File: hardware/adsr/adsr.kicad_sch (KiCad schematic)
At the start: 61 parts, among them J1 MonoJack, J2 MonoJack, J4 Conn_02x05_Odd_Even, Q1 BC847, Q2 BC847, Q3 BC847, Q4 BC847, Q5 BC847, Q6 2N7002K, SW1 SW_DPDT_x2, SW2 SW_Push, U1 ICM7556, U2 TL074

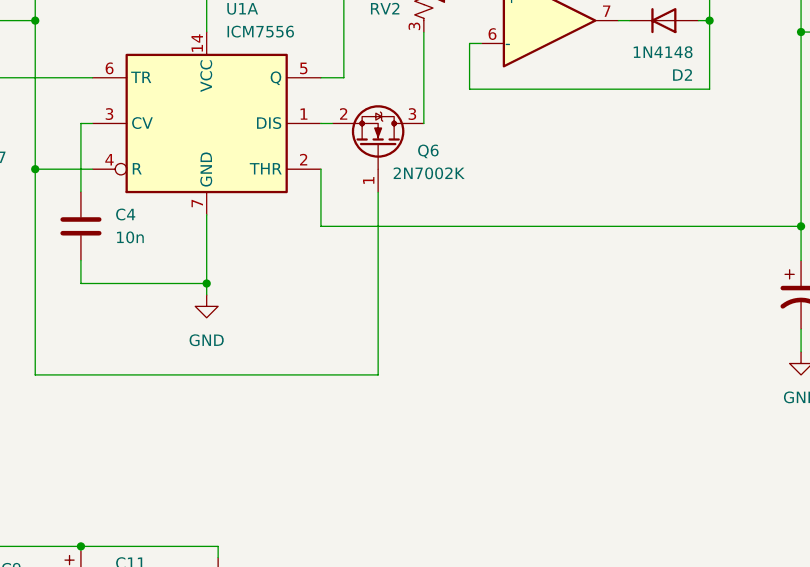
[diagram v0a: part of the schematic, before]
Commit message: Added missing gate R on MOSFET
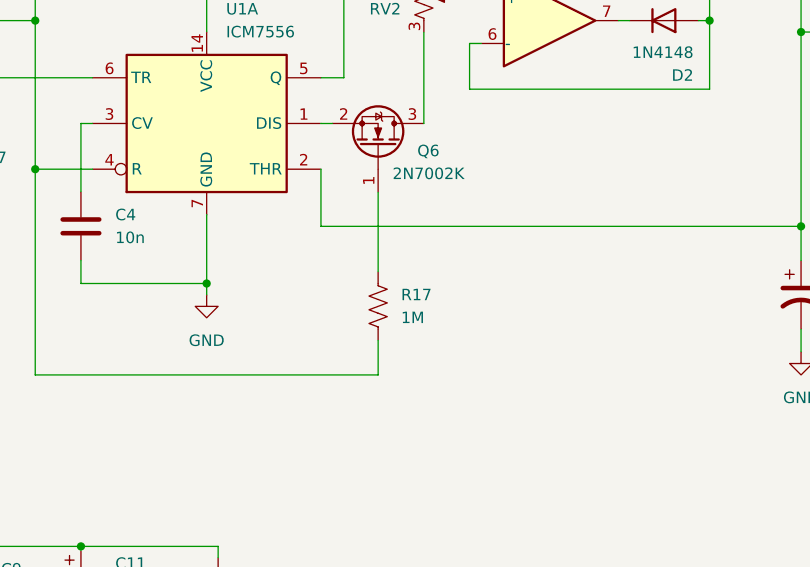
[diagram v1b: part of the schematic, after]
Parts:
- added R17: 1M, Resistor_SMD:R_0805_2012Metric_Pad1.20x1.40mm_HandSolder, symbol Device:R_US
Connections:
- net at C3.2, SW1.2 (B), U1.4 (R)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: now also R17.2; no longer Q6.1 (G)
- new net: Q6.1 (G), R17.1
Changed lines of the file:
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@@
 	(wire
 		(pts
+			(xy 180.34 137.16) (xy 180.34 128.27)
+		)
+		(stroke
+			(width 0)
+			(type default)
+		)
+	)
+	(wire
+		(pts
 			(xy 134.62 185.42) (xy 147.32 185.42)
 		)
@@
 	(wire
 		(pts
-			(xy 180.34 148.59) (xy 180.34 128.27)
+			(xy 180.34 148.59) (xy 180.34 144.78)
 		)
 		(stroke
@@
 					(unit 1)
 				)
+			)
+		)
+	)
+	(symbol
+		(lib_id "Device:R_US")
+		(at 180.34 140.97 0)
+		(unit 1)
+		(exclude_from_sim no)
+		(in_bom yes)
+		(on_board yes)
+		(dnp no)
+		(fields_autoplaced yes)
+		(property "Reference" "R17"
+			(at 182.88 139.6999 0)
+			(effects
+				(font
+					(size 1.27 1.27)
+				)
+				(justify left)
+			)
+		)
+		(property "Value" "1M"
+			(at 182.88 142.2399 0)
+			(effects
+				(font
+					(size 1.27 1.27)
+				)
+				(justify left)
+			)
+		)
+		(property "Footprint" "Resistor_SMD:R_0805_2012Metric_Pad1.20x1.40mm_HandSolder"
+			(at 181.356 141.224 90)
+			(effects
+				(font
+					(size 1.27 1.27)
+				)
+				(hide yes)
+			)
+		)
+		(property "Datasheet" "~"
+			(at 180.34 140.97 0)
+			(effects
+				(font
+					(size 1.27 1.27)
+				)
+				(hide yes)
+			)
+		)
+		(property "Description" "Resistor, US symbol"
+			(at 180.34 140.97 0)
+			(effects
+				(font
+					(size 1.27 1.27)
+				)
+				(hide yes)
+			)
+		)
+		(pin "1"
+		)
+		(pin "2"
+		)
+		(instances
+			(project "adsr"
+				(path "/bc327a33-f4cb-4cb8-a280-c2a5130340fc"
+					(reference "R17")
+					(unit 1)
+				)

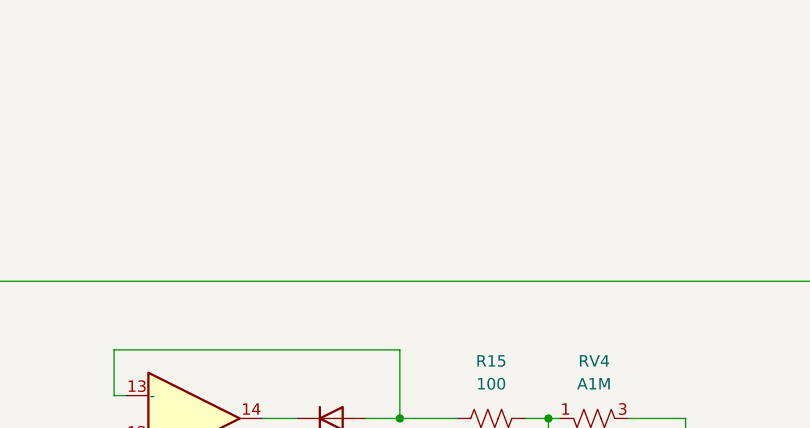
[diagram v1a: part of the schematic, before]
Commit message: added mechanical hole and final silk cleanup
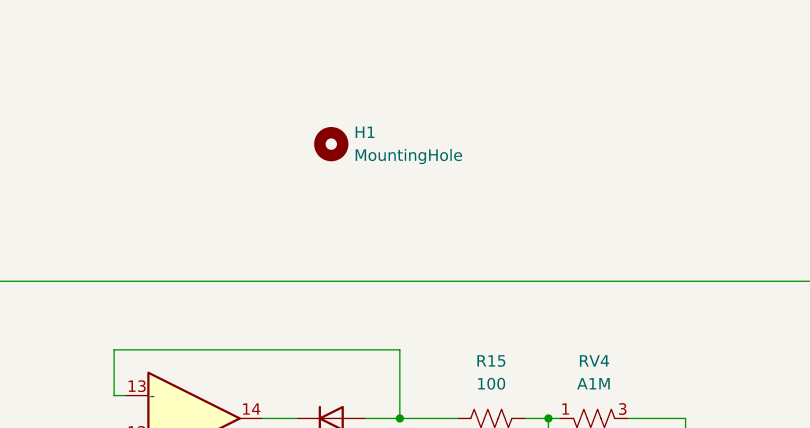
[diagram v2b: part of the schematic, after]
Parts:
- added H1: MountingHole, MountingHole:MountingHole_3.2mm_M3_DIN965, symbol Mechanical:MountingHole
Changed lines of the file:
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@@
+	)
+	(symbol
+		(lib_id "Mechanical:MountingHole")
+		(at 187.96 27.94 0)
+		(unit 1)
+		(exclude_from_sim no)
+		(in_bom no)
+		(on_board yes)
+		(dnp no)
+		(fields_autoplaced yes)
+		(property "Reference" "H1"
+			(at 190.5 26.6699 0)
+			(effects
+				(font
+					(size 1.27 1.27)
+				)
+				(justify left)
+			)
+		)
+		(property "Value" "MountingHole"
+			(at 190.5 29.2099 0)
+			(effects
+				(font
+					(size 1.27 1.27)
+				)
+				(justify left)
+			)
+		)
+		(property "Footprint" "MountingHole:MountingHole_3.2mm_M3_DIN965"
+			(at 187.96 27.94 0)
+			(effects
+				(font
+					(size 1.27 1.27)
+				)
+				(hide yes)
+			)
+		)
+		(property "Datasheet" "~"
+			(at 187.96 27.94 0)
+			(effects
+				(font
+					(size 1.27 1.27)
+				)
+				(hide yes)
+			)
+		)
+		(property "Description" "Mounting Hole without connection"
+			(at 187.96 27.94 0)
+			(effects
+				(font
+					(size 1.27 1.27)
+				)
+				(hide yes)
+			)
+		)
+		(instances
+			(project ""
+				(path "/bc327a33-f4cb-4cb8-a280-c2a5130340fc"
+					(reference "H1")
+					(unit 1)
+				)
+			)
+		)
 	)
 	(symbol

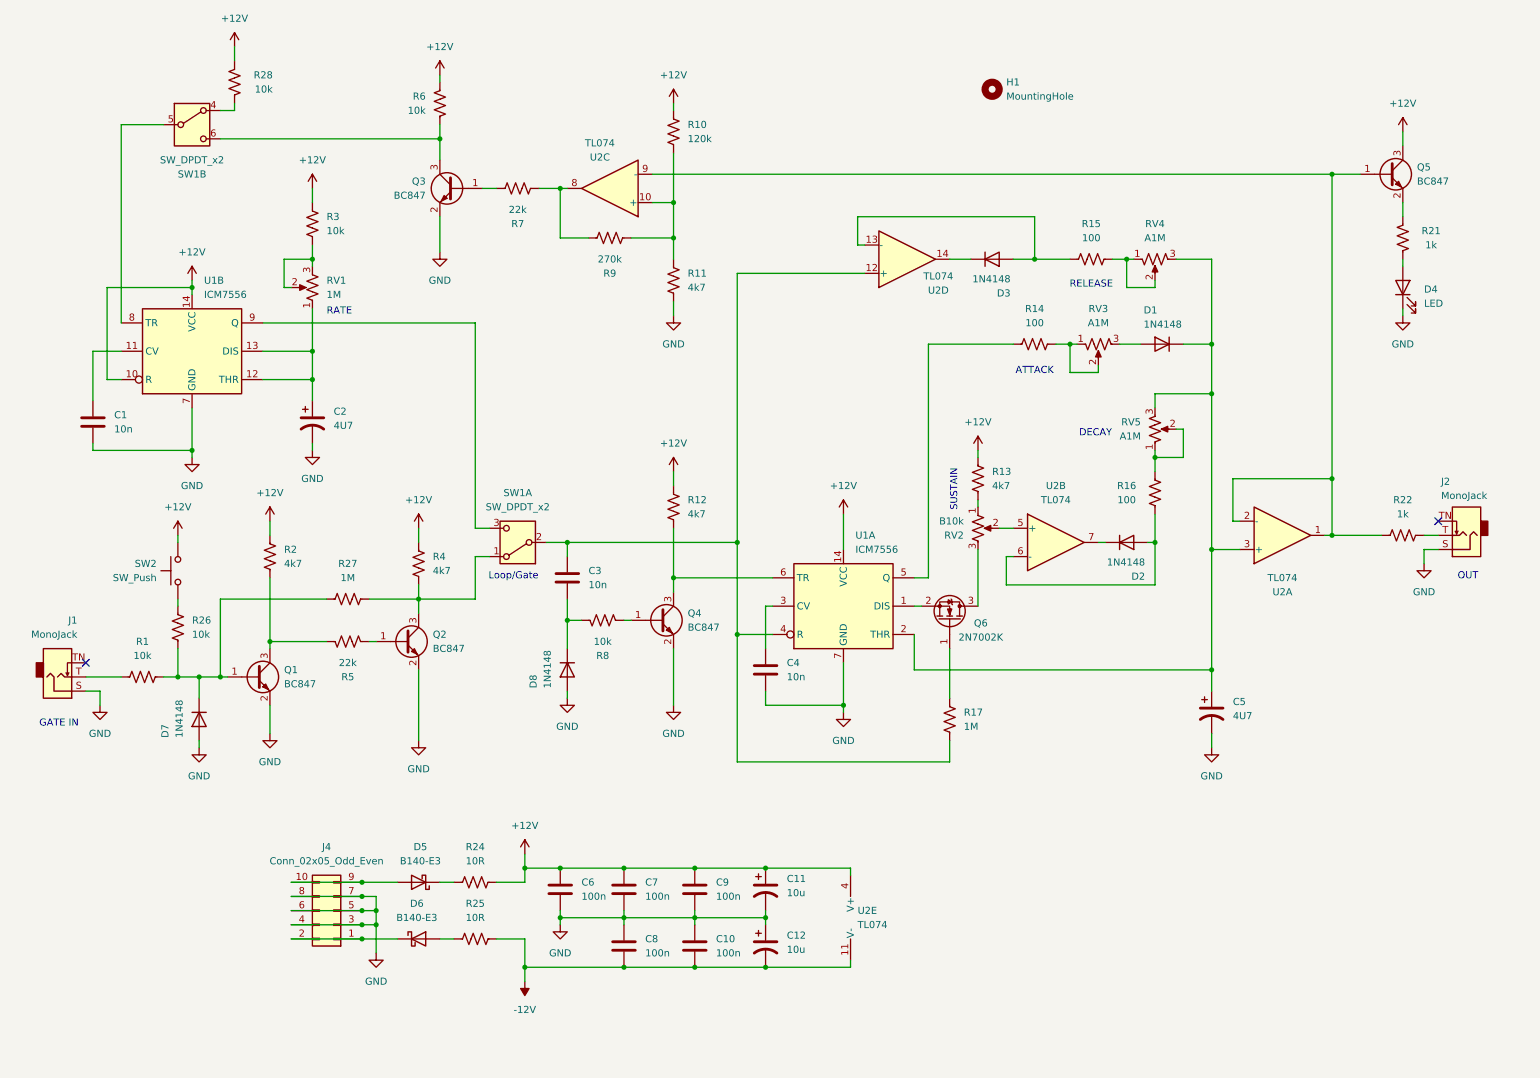
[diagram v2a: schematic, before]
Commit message: Committing WIP on ADSR with trigger: Falstad circuit & schematic, some changes to the KiCAD schematic (incomplete)
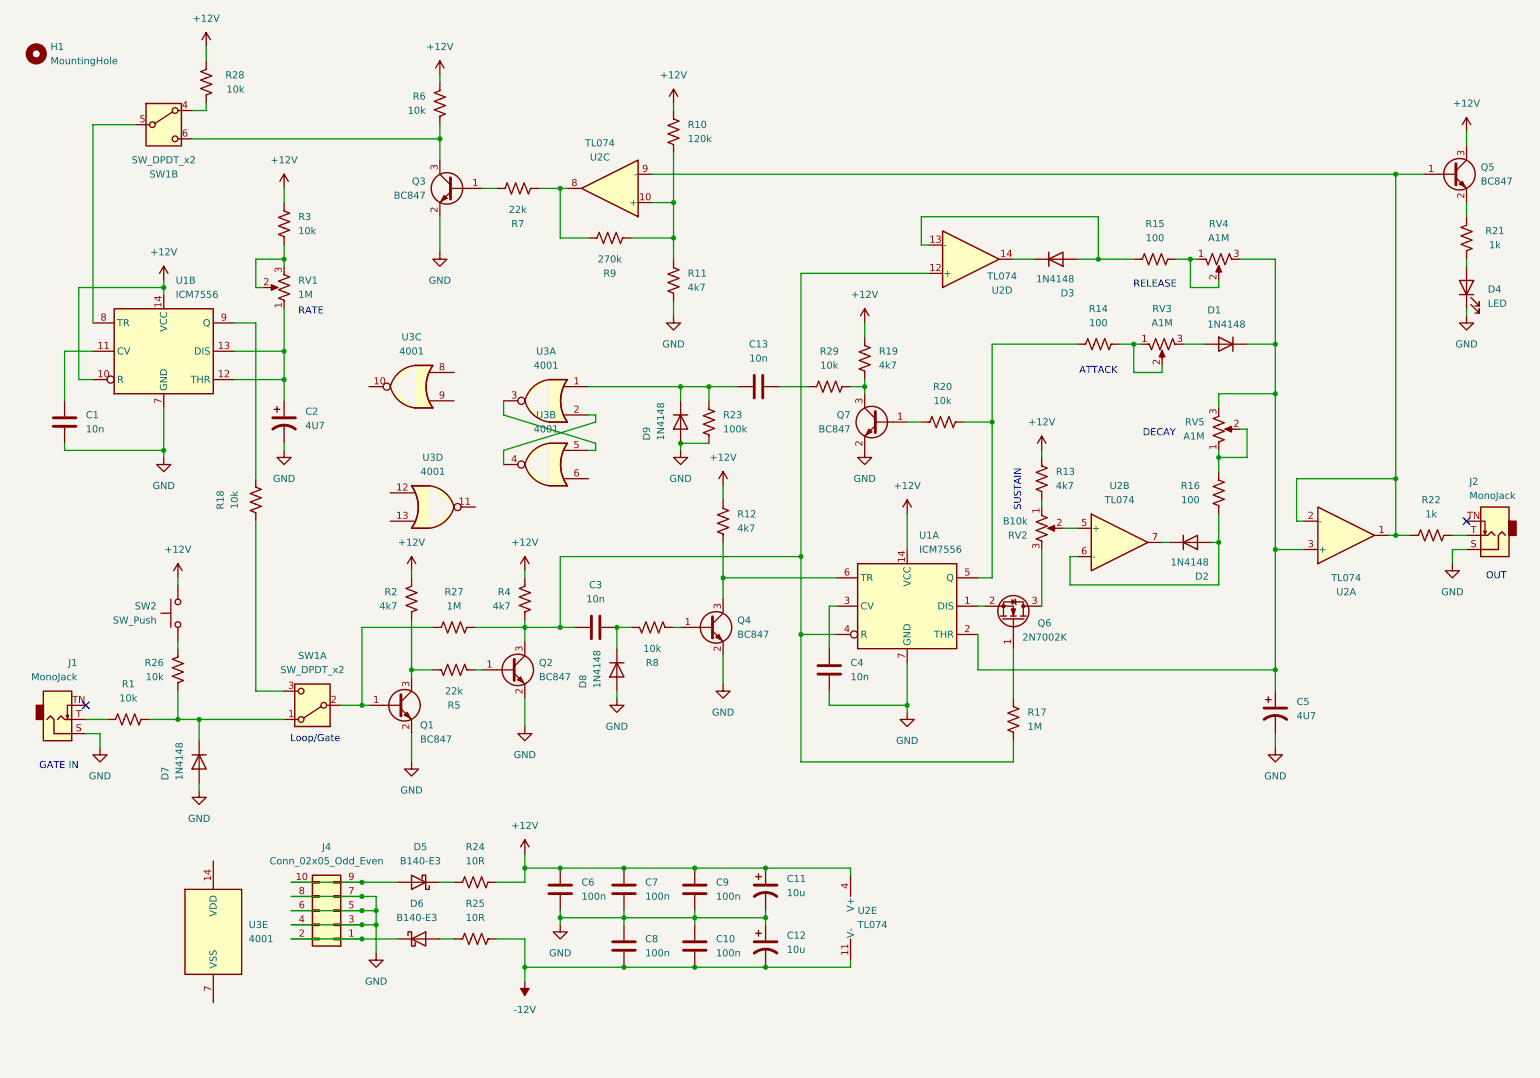
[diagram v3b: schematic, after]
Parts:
- added C13: 10n, Capacitor_SMD:C_0805_2012Metric_Pad1.18x1.45mm_HandSolder, symbol Device:C
- added D9: 1N4148, Diode_SMD:D_SOD-123, symbol Diode:1N4148
- added Q7: BC847, Package_TO_SOT_SMD:SOT-23, symbol Transistor_BJT:BC847
- added R18, R20, R29: 10k, Resistor_SMD:R_0805_2012Metric_Pad1.20x1.40mm_HandSolder, symbol Device:R_US
- added R19: 4k7, Resistor_SMD:R_0805_2012Metric_Pad1.20x1.40mm_HandSolder, symbol Device:R_US
- added R23: 100k, Resistor_SMD:R_0805_2012Metric_Pad1.20x1.40mm_HandSolder, symbol Device:R_US
- added U3: 4001, symbol 4xxx:4001
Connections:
- net +12V: now also R19.1
- net GND: now also D9.2 (A), Q7.2 (E), R23.2
- net at D7.1 (K), R1.2, R26.1: now also SW1.1 (A); no longer Q1.1 (B), R27.2
- net at Q2.3 (C), R27.1, R4.2: now also C3.2, R17.2, U1.4 (R), U2.12 (+); no longer SW1.1 (A)
- net at U1.9 (Q): now also R18.1; no longer SW1.3 (C)
- net at R14.1, U1.5 (Q): now also R20.2
- new net: C13.2, D9.1 (K), R23.1, U3.1
- new net: U3.2, U3.4
- new net: U3.3, U3.5
- new net: C13.1, R29.1
- new net: Q7.3 (C), R19.2, R29.2
- new net: Q1.1 (B), R27.2, SW1.2 (B)
- new net: R18.2, SW1.3 (C)
- new net: Q7.1 (B), R20.1
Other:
- moved on the sheet: C1, C2, C3, C4, C5, D1, D2, D3, D4, D7, D8, H1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

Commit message: schematic built and tested on breadboard
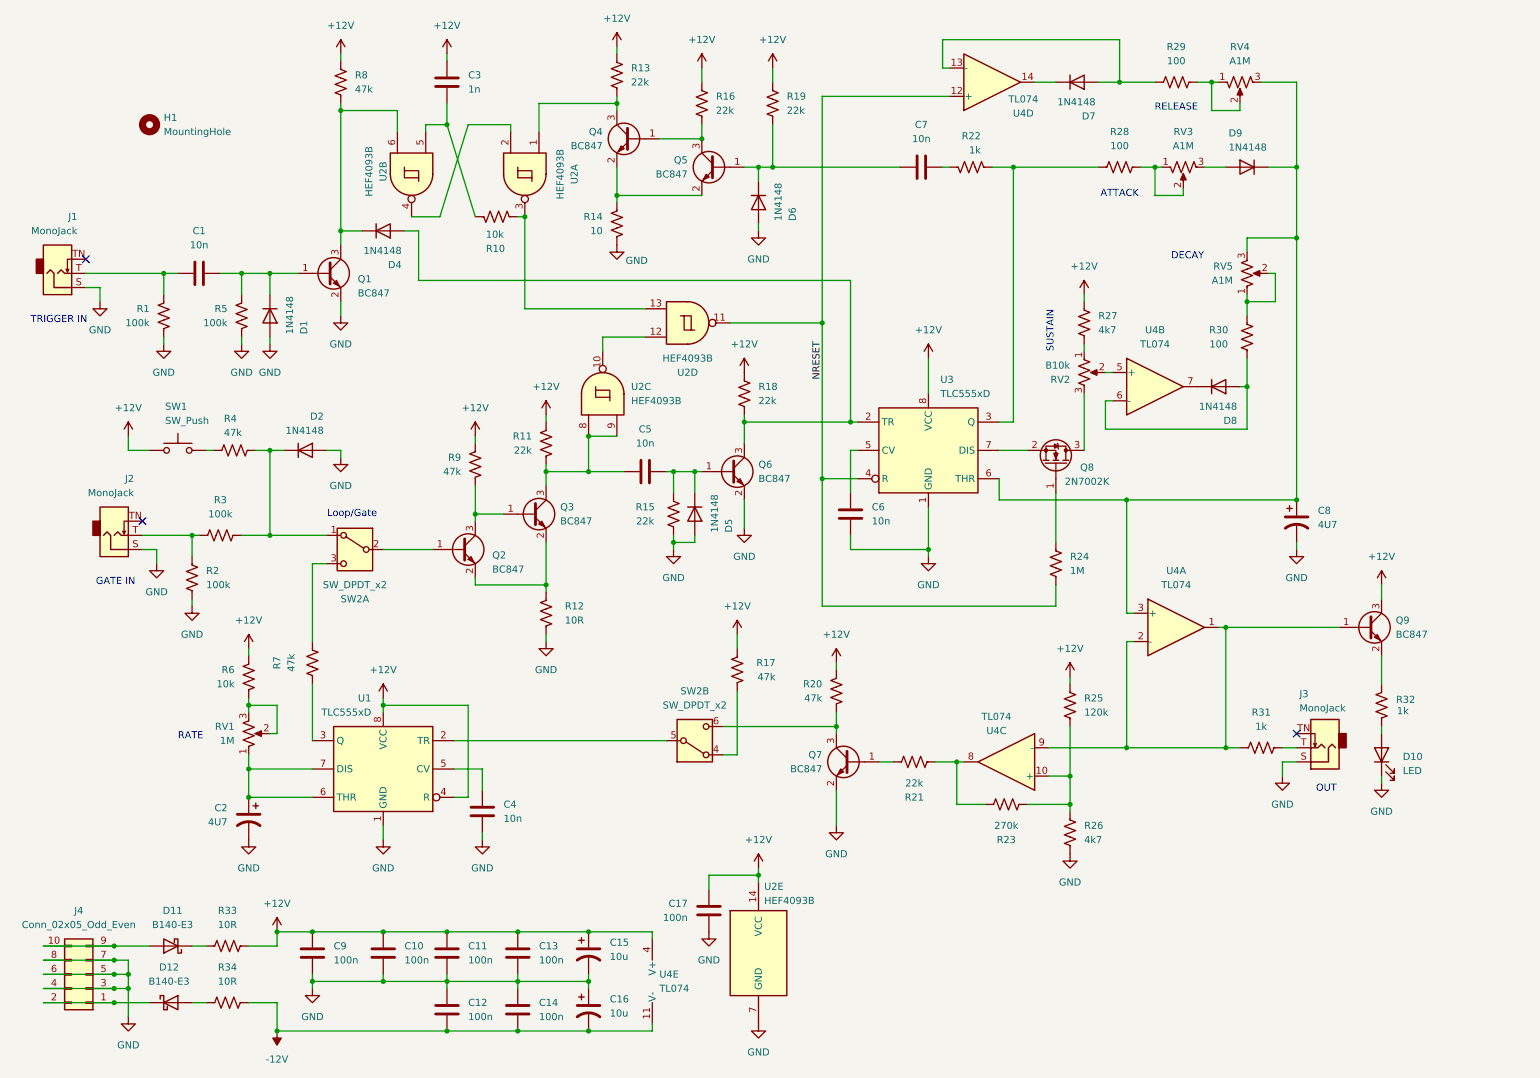
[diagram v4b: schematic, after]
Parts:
- removed D8, D9: 1N4148, Diode_SMD:D_SOD-123, symbol Diode:1N4148
- removed R23: 100k, Resistor_SMD:R_0805_2012Metric_Pad1.20x1.40mm_HandSolder, symbol Device:R_US
- removed R27: 1M, Resistor_SMD:R_0805_2012Metric_Pad1.20x1.40mm_HandSolder, symbol Device:R_US
- removed unit 2 of SW1
- removed U1: ICM7556, Package_SO:SOIC-14_3.9x8.7mm_P1.27mm, symbol Timer:ICM7556
- removed unit 1 of U2
- removed unit 3 of U2
- removed U3: 4001, symbol 4xxx:4001
- added C1: 10n, Capacitor_SMD:C_0805_2012Metric_Pad1.18x1.45mm_HandSolder, symbol Device:C
- added C10, C17: 100n, Capacitor_SMD:C_0805_2012Metric_Pad1.18x1.45mm_HandSolder, symbol Device:C
- added C3: 1n, Capacitor_SMD:C_0805_2012Metric_Pad1.18x1.45mm_HandSolder, symbol Device:C
- added D1, D4, D5, D6: 1N4148, Diode_SMD:D_SOD-123, symbol Diode:1N4148
- added J1: MonoJack, AudioJacks:Jack_3.5mm_QingPu_WQP-PJ301M-12_Vertical, symbol Connector_Audio:AudioJack2_SwitchT
- added Q1, Q5: BC847, Package_TO_SOT_SMD:SOT-23, symbol Transistor_BJT:BC847
- added R1, R2, R5: 100k, Resistor_SMD:R_0805_2012Metric_Pad1.20x1.40mm_HandSolder, symbol Device:R_US
- added R10: 10k, Resistor_SMD:R_0805_2012Metric_Pad1.20x1.40mm_HandSolder, symbol Device:R_US
- added R16, R19: 22k, Resistor_SMD:R_0805_2012Metric_Pad1.20x1.40mm_HandSolder, symbol Device:R_US
- added R8: 47k, Resistor_SMD:R_0805_2012Metric_Pad1.20x1.40mm_HandSolder, symbol Device:R_US
- added unit 2 of SW2
- added U1, U3: TLC555xD, Package_SO:SOIC-8_3.9x4.9mm_P1.27mm, symbol Timer:TLC555xD
- added U2: HEF4093B, Package_SO:SOIC-14_3.9x8.7mm_P1.27mm, symbol 4xxx:HEF4093B
- added unit 1 of U4
- added unit 3 of U4
- R11: renamed from R4; value 4k7 -> 22k
- R12: renamed from R5; value 22k -> 10R
- R13: renamed from R19; value 4k7 -> 22k
- R14: renamed from R20; value 10k -> 10
- R15: renamed from R8; value 10k -> 22k
- R17: renamed from R28; value 10k -> 47k
- R18: renamed from R12; value 4k7 -> 22k
- R20: renamed from R6; value 10k -> 47k
- R22: renamed from R29; value 10k -> 1k
- R3: renamed from R1; value 10k -> 100k
- R4: renamed from R26; value 10k -> 47k
- R7: renamed from R18; value 10k -> 47k
- R9: renamed from R2; value 4k7 -> 47k
- renumbered C7 to C11, C8 to C12, C9 to C13, C10 to C14, C11 to C15, C12 to C16, C1 to C4, C3 to C5, C4 to C6, C13 to C7, C5 to C8, C6 to C9, D4 to D10, D5 to D11, D6 to D12, D7 to D2, D3 to D7, D2 to D8, D1 to D9, J1 to J2, J2 to J3, Q1 to Q2, Q2 to Q3, Q7 to Q4, Q4 to Q6, Q3 to Q7, Q6 to Q8, Q5 to Q9, R7 to R21, R9 to R23, R17 to R24, R10 to R25, R11 to R26, R13 to R27, R14 to R28, R15 to R29, R16 to R30, R22 to R31, R21 to R32, R24 to R33, R25 to R34, R3 to R6, SW2 to SW1, SW1 to SW2, U2 to U4
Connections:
- net +12V: now also SW1.2, C10.2, C17.2, C3.2, R16.1, R19.1, R8.2, U1.4 (R), U1.8 (VCC), U2.14 (VCC), U3.8 (VCC); no longer SW1.1
- net GND: now also R12.2, R14.1, R15.2, C10.1, C17.1, D1.2 (A), D5.2 (A), D6.2 (A), J1.S, Q1.2 (E), R1.1, R2.1, R5.1, U1.1 (GND), U2.7 (GND), U3.1 (GND); no longer Q2.2 (E), Q3.2 (E), Q4.2 (E)
- net at Q9.1 (B), R31.1: now also U4.1, U4.2 (-), U4.9 (-)
- net at C8.1, D9.1 (K), RV4.3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: now also U3.6 (THR), U4.3 (+)
- net at J2.T, R3.1: now also R2.2
- net at R23.1, R25.1, R26.2: now also U4.10 (+)
- net at C4.2: now also U1.5 (CV)
- net at Q8.2 (S): now also U3.7 (DIS)
- net at C7.2: now also D6.1 (K), Q5.1 (B), R19.2
- net at Q4.3 (C), R13.2: now also U2.1; no longer R22.2
- net at Q3.1 (B): now also Q2.3 (C), R9.1; no longer R12.1
- net at C5.2, Q3.3 (C), R11.2: now also U2.8, U2.9; no longer R24.2, U4.12 (+)
- net at C2.1, RV1.1: now also U1.6 (THR), U1.7 (DIS)
- net at R7.1: now also SW2.3 (C)
- net at Q6.1 (B), R15.1: now also C5.1, D5.1 (K)
- net at Q6.3 (C), R18.2: now also D4.2 (A), U3.2 (TR)
- net at R21.2, R23.2: now also U4.8
- net at R7.2: now also U1.3 (Q); no longer SW2.3 (C)
- net at R28.1: now also R22.2, U3.3 (Q); no longer R14.2
- net at Q7.3 (C), R20.2: now also SW2.6 (C)
- net at R17.2: now also SW2.4 (A)
- net at Q4.1 (B): now also Q5.3 (C), R16.2; no longer R14.1
- net at R4.2: now also SW1.1; no longer SW1.2
- net at C6.2: now also U3.5 (CV)
- new net: C1.1, D1.1 (K), Q1.1 (B), R5.2
- new net: SW2.5 (B), U1.2 (TR)
- new net: Q2.2 (E), Q3.2 (E), R12.1
- new net: C3.1, R10.2, U2.5
- new net: U2.2, U2.4
- new net: R10.1, U2.13, U2.3
- new net: Q4.2 (E), Q5.2 (E), R14.2
- new net: U2.10, U2.12
- new net: C1.2, J1.T, R1.2
- new net: D4.1 (K), Q1.3 (C), R8.1, U2.6
- new net NRESET: R24.2, U2.11, U3.4 (R), U4.12 (+)
- no-connect marks 2 -> 3
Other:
- note added: "TRIGGER IN"
- moved on the sheet: C11, C12, C13, C14, C15, C16, C2, C4, C5, C6, C7, C8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
